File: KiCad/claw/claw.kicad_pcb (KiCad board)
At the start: 2 copper layers, 13 parts, among them J1 Molex_Spox_3pin, J2 Molex_Spox_3pin, J3 Molex_Spox_3pin, J4 Molex_Spox_3pin, J5 Molex_Spox_3pin, U1 ESP32_DEVKITV1, U2 TXS0108EPW, U3 74LS241

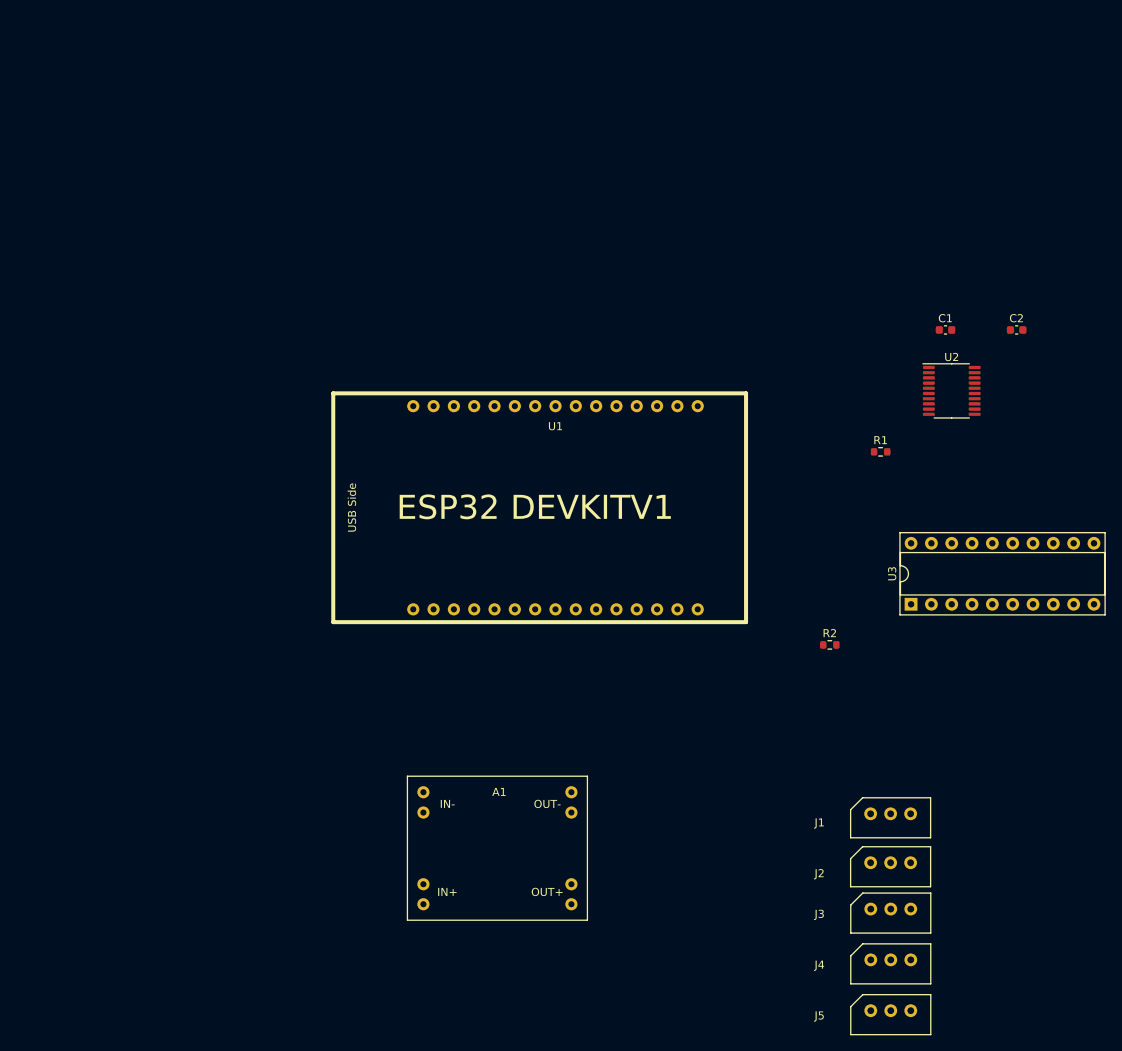
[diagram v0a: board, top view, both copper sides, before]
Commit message: added joystick connectors to schematic and layed out components on pcb
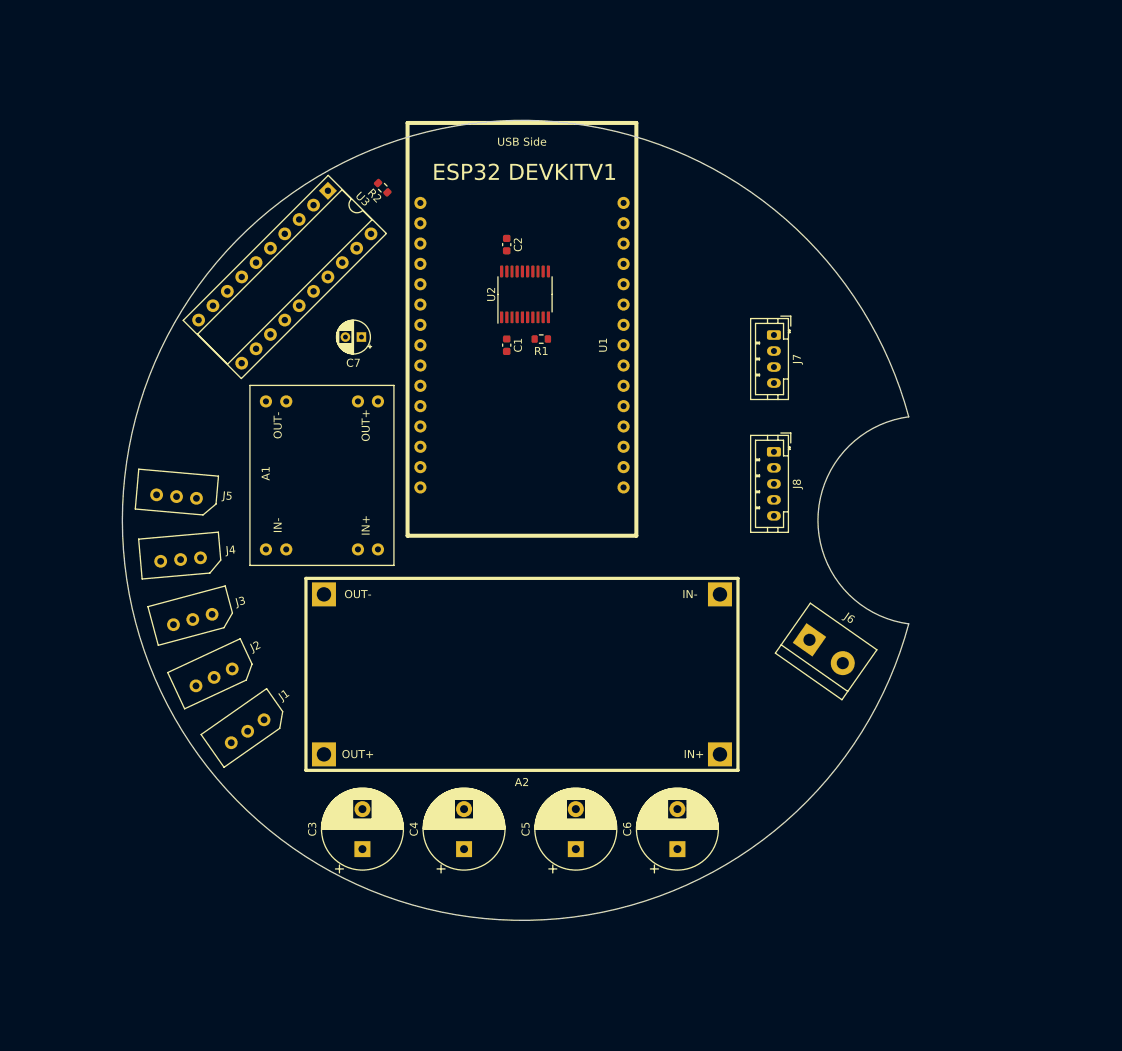
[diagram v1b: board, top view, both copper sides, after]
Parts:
- added A2: DC-DC_Buck, MyLib:DZS_Elec_DC-DC_Buck, F.Cu at (99.9, 119.3)
- added C3: 1000u, Capacitor_THT:CP_Radial_D10.0mm_P5.00mm, F.Cu at (80.0, 141.1)
- added C4: 1000u, Capacitor_THT:CP_Radial_D10.0mm_P5.00mm, F.Cu at (92.7, 141.1)
- added C5: 1000u, Capacitor_THT:CP_Radial_D10.0mm_P5.00mm, F.Cu at (106.7, 141.1)
- added C6: 1000u, Capacitor_THT:CP_Radial_D10.0mm_P5.00mm, F.Cu at (119.4, 141.1)
- added C7: 10u, Capacitor_THT:CP_Radial_D4.0mm_P2.00mm, F.Cu at (79.9, 77.1)
- added J6: Screw_Terminal_01x02, TerminalBlock:TerminalBlock_bornier-2_P5.08mm, F.Cu at (135.9, 114.9)
- added J7: Conn_01x04_Male, Connector_JST:JST_PH_B4B-PH-K_1x04_P2.00mm_Vertical, F.Cu at (131.4, 76.8)
- added J8: Conn_01x05_Male, Connector_JST:JST_PH_B5B-PH-K_1x05_P2.00mm_Vertical, F.Cu at (131.4, 91.4)
- moved J5 110.0 mm to (56.8, 97.0), turned to 175 degrees
- moved J4 101.9 mm to (57.3, 104.9), turned to 185 degrees
- moved J3 94.5 mm to (58.8, 112.4), turned to 195 degrees
- moved U3 89.4 mm to (75.7, 58.8), turned to 315 degrees
- moved J2 87.7 mm to (61.5, 119.6), turned to 205 degrees
- moved J1 81.0 mm to (65.7, 126.4), turned to 215 degrees
- moved R2 79.9 mm to (82.5, 58.4), turned to 135 degrees
- moved C2 64.6 mm to (98.0, 65.5), turned to 270 degrees
- moved C1 54.9 mm to (98.0, 78.1), turned to 270 degrees
- moved U2 54.7 mm to (100.3, 71.8), turned to 90 degrees
- moved R1 44.7 mm to (102.4, 77.3)
- moved A1 36.2 mm to (67.9, 103.6), turned to 90 degrees
- moved U1 20.7 mm to (99.9, 78.1), turned to 270 degrees
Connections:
- U1 pad 10: Net-(U1-Pad10) -> BUTTON
- U1 pad 20: Net-(U1-Pad20) -> POT_Z
- U1 pad 21: Net-(U1-Pad21) -> POT_Y
- U1 pad 22: Net-(U1-Pad22) -> POT_X
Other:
- board outline added: 98.3 x 100 mm

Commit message: pcb traces
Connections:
- U1 pad 29: Net-(U1-Pad29) -> GND
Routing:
- net +5V: track 0.00 -> 104.1 mm
- net +12V: track 0.00 -> 103.0 mm
- net +3V3: track 0.00 -> 100.5 mm, vias 0 -> 2
- net GND: track 0.00 -> 91.5 mm, vias 0 -> 3
- net MOTOR_SIGNAL: track 0.00 -> 90.0 mm
- net +8V: track 0.00 -> 85.1 mm
- net BUTTON: track 0.00 -> 49.3 mm
- net DIR_5V: track 0.00 -> 32.7 mm, vias 0 -> 1
- net DIR_3V3: track 0.00 -> 25.2 mm, vias 0 -> 2
- net TX_5V: track 0.00 -> 24.6 mm
- net POT_Z: track 0.00 -> 22.5 mm
- net RX_5V: track 0.00 -> 21.1 mm
- net POT_Y: track 0.00 -> 18.9 mm
- net POT_X: track 0.00 -> 18.9 mm
- net TX_3V3: track 0.00 -> 17.8 mm
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- added copper zone on B.Cu, net GND
- added copper zone on F.Cu, net GND
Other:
- rule via_min_drill: 0.3 -> 0.2
- board text added: "+12V"
- board text added: "3V3"
- board text added: "BTN"
- board text added: "GND"
- board text added: "POT_X"
- board text added: "POT_Y"
- board text added: "POT_Z"

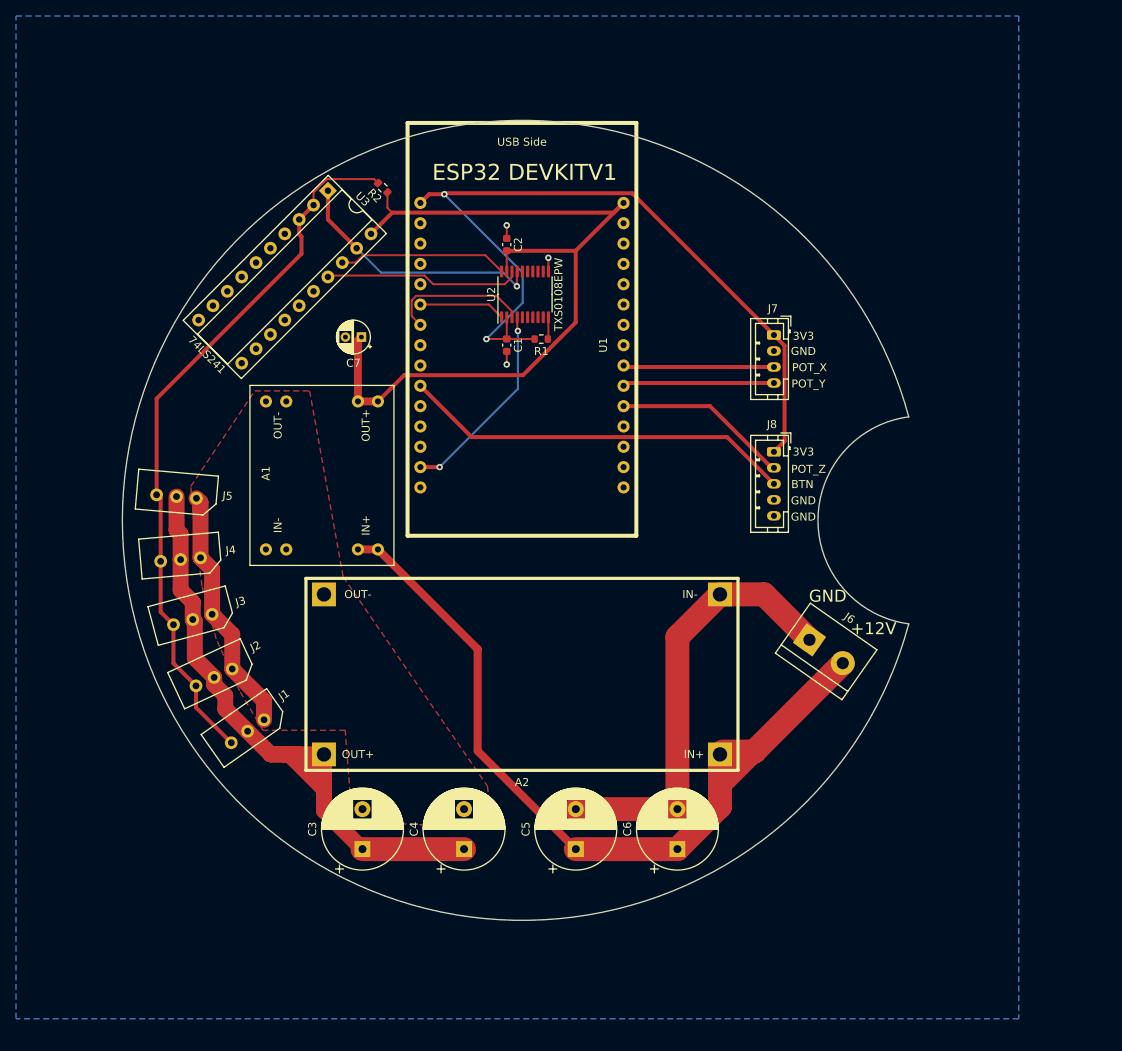
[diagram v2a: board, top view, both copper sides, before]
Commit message: added PCB mounting holes
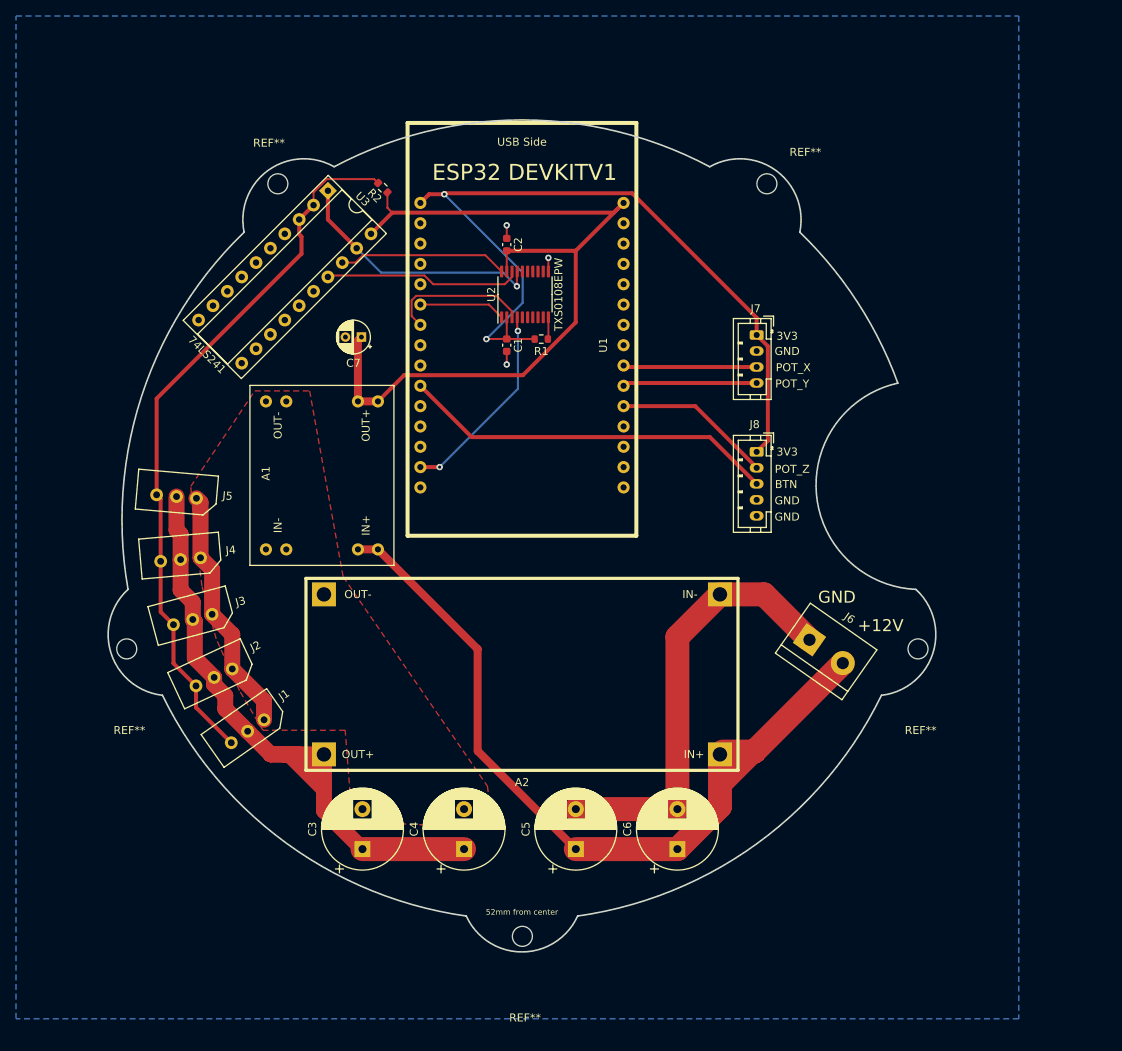
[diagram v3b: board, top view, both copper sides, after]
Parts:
- added REF**: MountingHole_2.5mm, MountingHole:MountingHole_2.5mm, F.Cu at (50.5, 116.1)
- added REF**: MountingHole_2.5mm, MountingHole:MountingHole_2.5mm, F.Cu at (69.4, 57.9)
- added REF**: MountingHole_2.5mm, MountingHole:MountingHole_2.5mm, F.Cu at (130.6, 57.9)
- added REF**: MountingHole_2.5mm, MountingHole:MountingHole_2.5mm, F.Cu at (149.5, 116.1)
- added REF**: MountingHole_2.5mm, MountingHole:MountingHole_2.5mm, F.Cu at (100.0, 152.0)
- moved J7 2.16 mm to (129.3, 76.8)
- moved J8 2.16 mm to (129.3, 91.4)
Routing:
- net POT_Z: track 22.5 -> 19.9 mm
- net BUTTON: track 49.3 -> 47.1 mm
- net POT_Y: track 18.9 -> 16.8 mm
- net POT_X: track 18.9 -> 16.7 mm
- net +3V3: track 100.5 -> 99.7 mm
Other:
- board size 98.3 x 100 mm -> 103.5 x 104 mm
- board text added: "52mm from center"

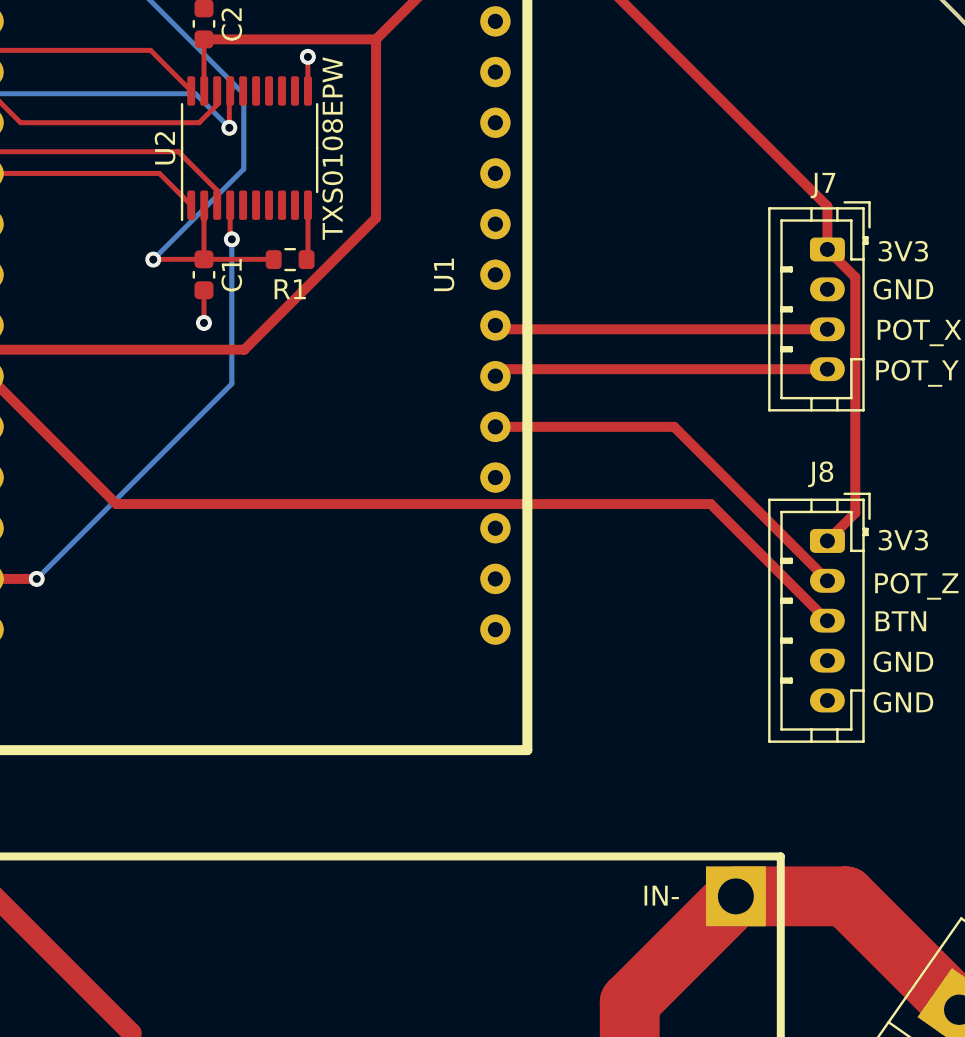
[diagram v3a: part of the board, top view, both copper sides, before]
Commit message: updated finger offsets
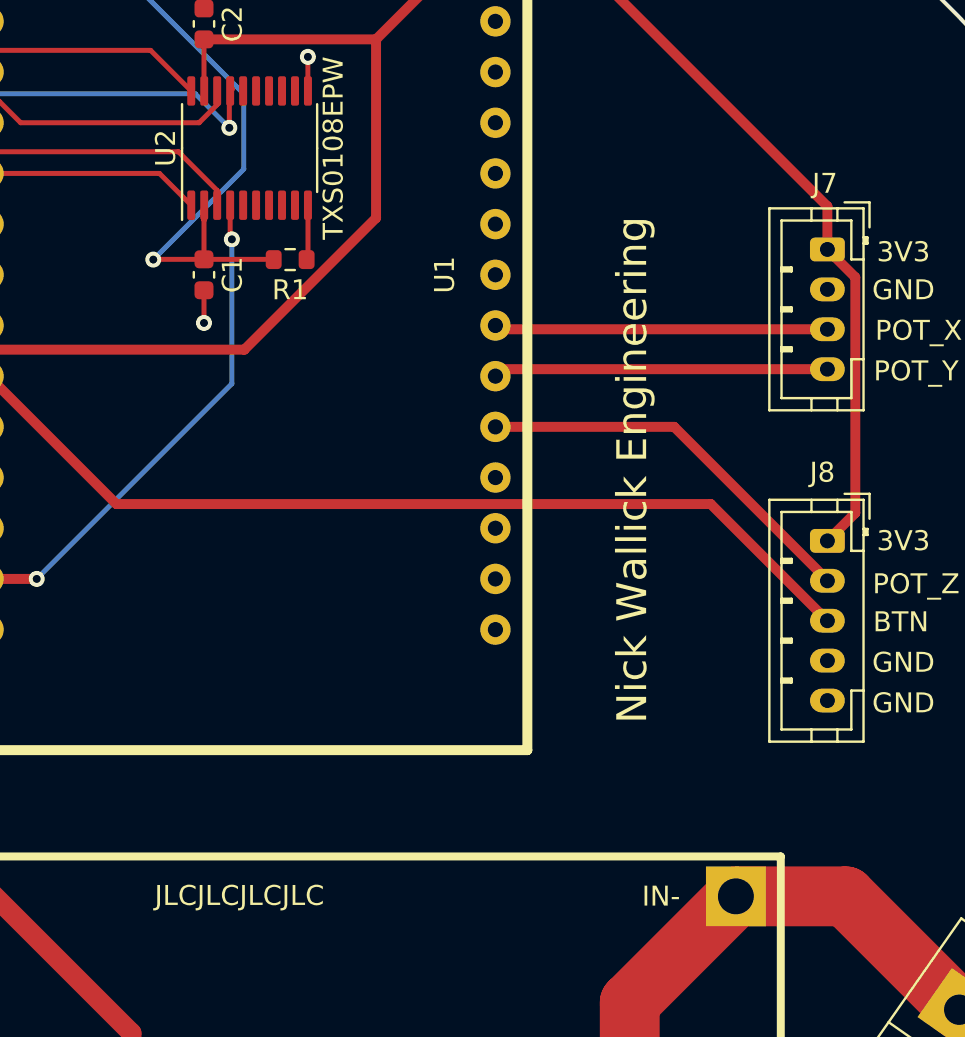
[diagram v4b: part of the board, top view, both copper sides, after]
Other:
- board text added: "JLCJLCJLCJLC"
- board text added: "Nick Wallick Engineering"
